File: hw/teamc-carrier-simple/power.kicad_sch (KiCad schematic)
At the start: 20 parts, among them J22 PWR toggle, J23 charger BAT+/BAT-, U2 Pololu U3V70F5 5V boost, U3 Pololu ideal diode 20A, U4 MCP1700-3302E/TO, U6 Adafruit MAX17048 fuel gauge

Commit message: Carrier rev C (simple): checkpoint 3 - placed and routed on one copper layer, DRC 0/0/0, 4 wire links
120 x 66 mm (box not measured yet: hw/scripts/layout_carrier_simple.py rebuilds everything after the
outline in place_carrier_simple.py changes). Backbone hand-routed (route_carrier_simple.py), router for
the short branches, GND pour; DRC with schematic parity 0 violations / 0 unconnected / 0 parity, all
severities; ERC 0/0. Tracks 0.8-2.0 mm. Wire links: IRQ over CSN and three ground pockets. Crossings by
tracks between resistor legs (SCK under R84/R83, LED_ACT_A under R61, CSN/IRQ under R57).
Layout-driven schematic changes: input 100 nF caps dropped, C18 at the toggle lead, 7.62 mm resistor
pitch, D1 on 12.7 mm, three M3 holes. Cable-tie slot + edge notch at the cell. 3D models for the
modules, wire links, holder, fuse clips and test points (gen_3d_revc.py; fetch_3d substitutes).
Fab: F.Cu + Edge.Cuts gerbers, drill, 1:1 copper PDFs, assembly PDFs, wire_links.csv, zip; renders.

Co-Authored-By: Claude Opus 5.5 <noreply@anthropic.com>
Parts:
- D1: footprint Diode_THT:D_DO-201AD_P15.24mm_Horizontal -> Diode_THT:D_DO-201AD_P12.70mm_Horizontal
- R9: footprint teamc:R_Axial_DIN0207_L6.3mm_D2.5mm_P10.16mm_Horizontal_Pad1.8mm -> teamc:R_Axial_DIN0207_L6.3mm_D2.5mm_P7.62mm_Horizontal_Pad1.8mm
- U2: footprint teamc:Pololu_U3V70F5_Headers -> teamc:RevC_Pololu_U3V70F5_Headers
- U3: footprint teamc:Pololu_IdealDiode_5388_Headers -> teamc:RevC_Pololu_IdealDiode_5388_Headers
- U6: footprint teamc:Adafruit_MAX17048_5580_Headers -> teamc:RevC_Adafruit_MAX17048_5580_Headers
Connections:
- net PWR_EN: no longer C18.1
- net PWR_SW_J: now also C18.1
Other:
- note added: "Toggle CLOSED = ENABLE pulled to GND = boost asleep = box OFF (the battery current never goes through the switch). Toggle OPEN = the module's own 100 k pull-up wakes it = box ON. A lead that breaks in the drop test therefore leaves the box running. Mount the toggle so that 'down' (closed) is marked OFF. C18 + R9: 100 nF at the lead, then 1 k to ENABLE: a zap on the lever goes into C18, R9 limits 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"
- note removed: "Toggle CLOSED = ENABLE pulled to GND = boost asleep = box OFF (the battery current never goes through the switch). Toggle OPEN = the module's own 100 k pull-up wakes it = box ON. A lead that breaks in the drop test therefore leaves the box running. Mount the toggle so that 'down' (closed) is marked OFF. R9 + C18: the same 1 k + 100 nF filter as every panel lead (noise and a zap from the metal lev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"
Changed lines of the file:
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@@
 			)
 		)
-		(property "Footprint" "Diode_THT:D_DO-201AD_P15.24mm_Horizontal"
+		(property "Footprint" "Diode_THT:D_DO-201AD_P12.70mm_Horizontal"
 			(at 86.36 50.8 0)
 			(effects
@@
 			)
 		)
-		(property "Footprint" "teamc:R_Axial_DIN0207_L6.3mm_D2.5mm_P10.16mm_Horizontal_Pad1.8mm"
+		(property "Footprint" "teamc:R_Axial_DIN0207_L6.3mm_D2.5mm_P7.62mm_Horizontal_Pad1.8mm"
 			(at 325.12 38.1 0)
 			(effects
@@
 		)
 	)
-	(label "PWR_EN"
+	(label "PWR_SW_J"
 		(at 339.09 50.8 180)
 		(fields_autoplaced yes)
@@
 			)
 		)
-		(property "Footprint" "teamc:Pololu_U3V70F5_Headers"
+		(property "Footprint" "teamc:RevC_Pololu_U3V70F5_Headers"
 			(at 55.88 147.32 0)
 			(effects
@@
 			)
 		)
-		(property "Footprint" "teamc:Pololu_IdealDiode_5388_Headers"
+		(property "Footprint" "teamc:RevC_Pololu_IdealDiode_5388_Headers"
 			(at 190.5 147.32 0)
 			(effects
@@
 			)
 		)
-		(property "Footprint" "teamc:Adafruit_MAX17048_5580_Headers"
+		(property "Footprint" "teamc:RevC_Adafruit_MAX17048_5580_Headers"
 			(at 190.5 231.14 0)
 			(effects
@@
 		)
 	)
-	(text "Toggle CLOSED = ENABLE pulled to GND = boost asleep = box OFF (the battery current never goes through\nthe switch). Toggle OPEN = the module's own 100 k pull-up wakes it = box ON. A lead that breaks in the drop\ntest therefore leaves the box running. Mount the toggle so that 'down' (closed) is marked OFF.\nR9 + C18: the same 1 k + 100 nF filter as every panel lead (noise and a zap from the metal lever).\nWith the toggle closed: EN = VBAT x 1k / 101k = 0.04 V (< 0.4 V needed). Off drain: ~40 uA in the pull-up."
+	(text "Toggle CLOSED = ENABLE pulled to GND = boost asleep = box OFF (the battery current never goes through\nthe switch). Toggle OPEN = the module's own 100 k pull-up wakes it = box ON. A lead that breaks in the drop\ntest therefore leaves the box running. Mount the toggle so that 'down' (closed) is marked OFF.\nC18 + R9: 100 nF at the lead, then 1 k to ENABLE: a zap on the lever goes into C18, R9 limits what reaches\nthe module (C18 sits at the connector since checkpoint 3: room on the board).\nWith the toggle closed: EN = VBAT x 1k / 101k = 0.04 V (< 0.4 V needed). Off drain: ~40 uA in the pull-up."
 		(exclude_from_sim no)
 		(at 287.02 63.5 0)

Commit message: Carrier rev C (simple): checkpoint-3 fixes (P4KE10A TVS per panel lead, wire-loop test points), board 120 x 68 mm, build guide and shopping list
- D12-D16 P4KE10A (DO-41 standing) at the panel-lead connectors; TP2/TP3/TP4 low wire loops (TP2/TP4 under the breakout)
- J13 UART order kept as rev A/B (1 GND, 2 TX, 3 RX); ui.py docstring fixed
- layout: TVS rows, R56/CSN lowered, board 66 -> 68 mm so the GND pour keeps a >= 1.9 mm channel between its halves
- own 3D stand-in for the 3.81 mm vertical DO-41 (none upstream); ERC 0/0, DRC 0/0/0, 4 wire links, renders resolved
- hw/REVC_GUIDE.md, hw/REVC_SHOPPING.md, DESIGN_NOTES rev C section, BoM EUR 145.51/box; reviewer fixes in the guide

Co-Authored-By: Claude Opus 5.5 <noreply@anthropic.com>
Claude-Session: https://claude.ai/code/session_01PKzvcoWGaf5niy6TrXYsya
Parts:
- added D16: P4KE10A TVS, Diode_THT:D_DO-41_SOD81_P3.81mm_Vertical_CathodeUp, symbol Device:D_Zener
- TP2, TP4: footprint TestPoint:TestPoint_Keystone_5010-5014_Multipurpose -> TestPoint:TestPoint_Loop_D2.50mm_Drill1.0mm; MPN 5010 (red) -> wire loop (bare tinned wire, ~3 mm high); Manufacturer Keystone -> (none)
- TP3: footprint TestPoint:TestPoint_Keystone_5010-5014_Multipurpose -> TestPoint:TestPoint_Loop_D2.50mm_Drill1.0mm; MPN 5011 (black) -> wire loop (bare tinned wire, ~3 mm high); Manufacturer Keystone -> (none)
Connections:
- net GND: now also D16.2 (A)
- net PWR_SW_J: now also D16.1 (K)
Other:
- note added: "TP1 VBAT 3.0-4.2 V · TP2 5V_PI 4.8-5.2 V · TP4 3V3_RADIO 3.2-3.4 V · TP3 GND (black). Measure all of them BEFORE plugging in the ribbon (Pi) and the radio breakout. TP2/TP4 are low wire loops (~5 mm) under the breakout's place (a Keystone 5010 is too tall there); TP3 (GND) is a loop too, beside TP1."
- note removed: "TP1 VBAT 3.0-4.2 V · TP2 5V_PI 4.8-5.2 V · TP4 3V3_RADIO 3.2-3.4 V · TP3 GND (black). Measure all of them BEFORE plugging in the ribbon (Pi) and the radio breakout."

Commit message: Rev C: order-ready DigiKey cart + order check; C1/C9 -> KEMET ESS107M016AE2EA, red LED -> WP7113SURDK
- hw/teamc-carrier-simple/order/: digikey_cart.csv (BOM Manager upload, 3 boards incl.
  spares), order_check.md (per-line PN/stock/price, 24-Oct), other_shops.md (Kiwi, nkon,
  TP4056 options).
- EEU-FR1C101 is 5 mm / 2.0 mm leads and did not fit the 6.3 mm / 2.5 mm footprint; the
  exact Panasonic is out of stock until Dec -> KEMET ESS107M016AE2EA (C1/C9 sit outside
  the breakout area, 8.5 mm tall is fine). WP7113ID out of stock -> WP7113SURDK.
- Standoffs, nylon screws and LED clips sourced at DigiKey; cell (nkon) and ribbon (Kiwi)
  linked. BoM EUR 148.00/box. REVC_SHOPPING.md: how to order + what is still open.
- Rebuilt: ERC 0, DRC 0/0/0, 4 wire links.

Co-Authored-By: Claude Opus 5.5 <noreply@anthropic.com>
Claude-Session: https://claude.ai/code/session_01PKzvcoWGaf5niy6TrXYsya
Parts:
- C1, C9: MPN EEU-FR1C101 -> ESS107M016AE2EA; Manufacturer Panasonic -> KEMET
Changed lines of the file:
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@@
 			)
 		)
-		(property "MPN" "EEU-FR1C101"
+		(property "MPN" "ESS107M016AE2EA"
 			(at 111.76 50.8 0)
 			(effects
@@
 			)
 		)
-		(property "Manufacturer" "Panasonic"
+		(property "Manufacturer" "KEMET"
 			(at 111.76 50.8 0)
 			(effects
@@
 			)
 		)
-		(property "MPN" "EEU-FR1C101"
+		(property "MPN" "ESS107M016AE2EA"
 			(at 241.3 139.7 0)
 			(effects
@@
 			)
 		)
-		(property "Manufacturer" "Panasonic"
+		(property "Manufacturer" "KEMET"
 			(at 241.3 139.7 0)
 			(effects

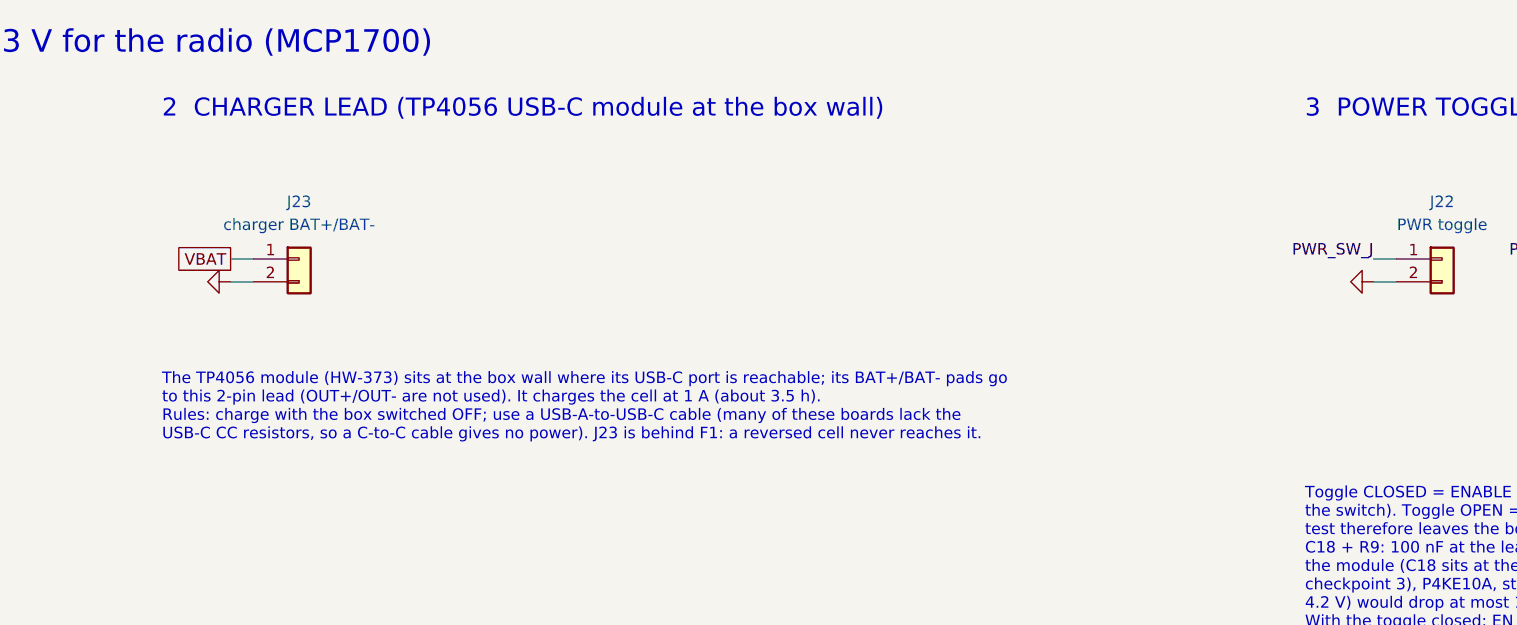
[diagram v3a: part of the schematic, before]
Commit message: Rev C order: Adafruit #4410 charger in the DigiKey cart, Pi M2.5 kit from Kiwi, switches from TME
No TP4056 USB-C board with protection was orderable on 24-Oct (TinyTronics 2-4 weeks,
Grobotronics/Electrokit out, Amazon.es 3-pack apparently out). Santiago chose the Adafruit
Micro-Lipo USB-C #4410 (DigiKey 1528-4410-ND, 966 in stock; 500 mA jumper, ~7-8 h; the
protected 18650 has its own protection). That put the box at EUR 150.45, so the panel
switches move to TME (his budget lever) -> EUR 148.29/box. Pi standoffs: Kiwi KW-2754 nylon
M2.5 set (DigiKey M2.5 screws removed from the cart).
Cart, other_shops.md, order_check.md (update section), REVC_SHOPPING.md (four orders,
~EUR 253 excl. for 3 boards), guide (charger jumper/wiring/charging), schematic note, BoM,
CONCEPT, CLAUDE.md. Rebuilt: ERC 0, DRC 0/0/0, 4 links.

Co-Authored-By: Claude Opus 5.5 <noreply@anthropic.com>
Claude-Session: https://claude.ai/code/session_01PKzvcoWGaf5niy6TrXYsya
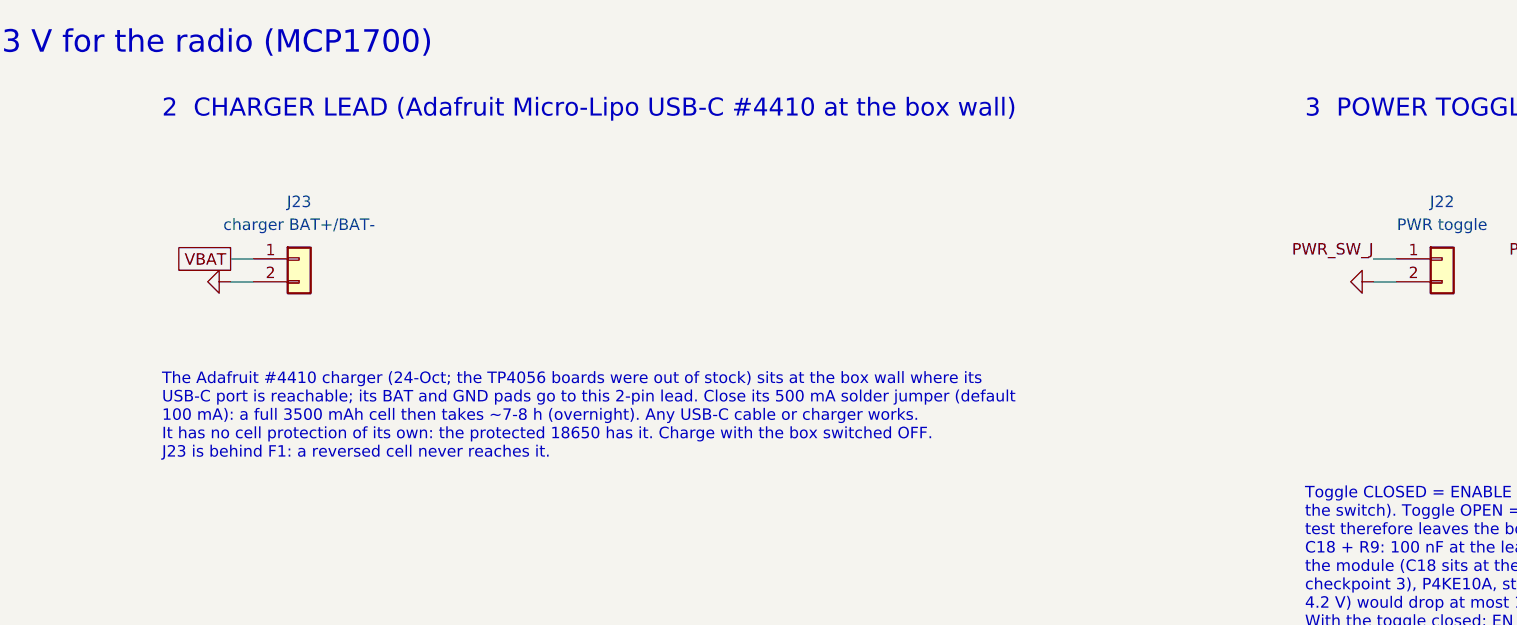
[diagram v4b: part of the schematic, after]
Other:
- note added: "2 CHARGER LEAD (Adafruit Micro-Lipo USB-C #4410 at the box wall)"
- note added: "The Adafruit #4410 charger (24-Oct; the TP4056 boards were out of stock) sits at the box wall where its USB-C port is reachable; its BAT and GND pads go to this 2-pin lead. Close its 500 mA solder jumper (default 100 mA): a full 3500 mAh cell then takes ~7-8 h (overnight). Any USB-C cable or charger works. It has no cell protection of its own: the protected 18650 has it. Charge with the box switc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"
- note removed: "2 CHARGER LEAD (TP4056 USB-C module at the box wall)"
- note removed: "The TP4056 module (HW-373) sits at the box wall where its USB-C port is reachable; its BAT+/BAT- pads go to this 2-pin lead (OUT+/OUT- are not used). It charges the cell at 1 A (about 3.5 h). Rules: charge with the box switched OFF; use a USB-A-to-USB-C cable (many of these boards lack the USB-C CC resistors, so a C-to-C cable gives no power). J23 is behind F1: a reversed cell never reaches it."
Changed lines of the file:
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@@
 		)
 	)
-	(text "2  CHARGER LEAD (TP4056 USB-C module at the box wall)"
+	(text "2  CHARGER LEAD (Adafruit Micro-Lipo USB-C #4410 at the box wall)"
 		(exclude_from_sim no)
 		(at 160.02 20.32 0)
@@
 		)
 	)
-	(text "The TP4056 module (HW-373) sits at the box wall where its USB-C port is reachable; its BAT+/BAT- pads go\nto this 2-pin lead (OUT+/OUT- are not used). It charges the cell at 1 A (about 3.5 h).\nRules: charge with the box switched OFF; use a USB-A-to-USB-C cable (many of these boards lack the\nUSB-C CC resistors, so a C-to-C cable gives no power). J23 is behind F1: a reversed cell never reaches it."
+	(text "The Adafruit #4410 charger (24-Oct; the TP4056 boards were out of stock) sits at the box wall where its\nUSB-C port is reachable; its BAT and GND pads go to this 2-pin lead. Close its 500 mA solder jumper (default\n100 mA): a full 3500 mAh cell then takes ~7-8 h (overnight). Any USB-C cable or charger works.\nIt has no cell protection of its own: the protected 18650 has it. Charge with the box switched OFF.\nJ23 is behind F1: a reversed cell never reaches it."
 		(exclude_from_sim no)
 		(at 160.02 50.8 0)
